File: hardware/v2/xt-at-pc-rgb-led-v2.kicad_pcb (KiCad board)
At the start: 2 copper layers, 54.5 x 33 mm, 25 parts, among them J1 +5V GND, J2 HDD, J3 TURBO, J4 SW IN, J5 SW OUT, J6 ADDR LED (5V DATA GND), J7 RGB LED (COM R G B), J8 ISP, U1 ATtiny84A-PU

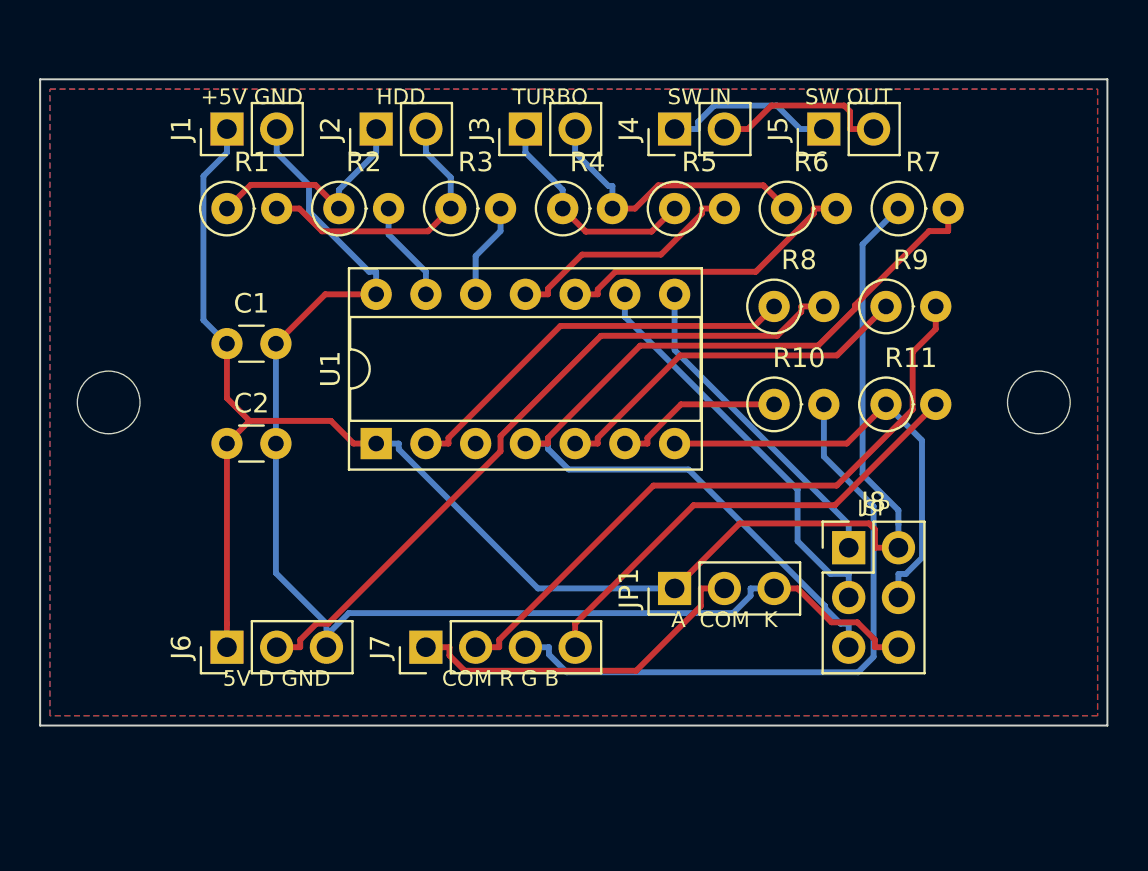
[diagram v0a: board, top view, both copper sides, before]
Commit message: v2: mounting holes between parts, board 42.5 x 33 mm
C2 and R11 moved so the M3 holes fit between the parts; board width
54.5 -> 42.5 mm. Dimension drawings assume standing resistors (about
11 mm height).

Co-Authored-By: Claude Opus 5.5 (1M context) <noreply@anthropic.com>
Claude-Session: https://claude.ai/code/session_01JRatMm8Q7Nvo5CN8dD4gBk
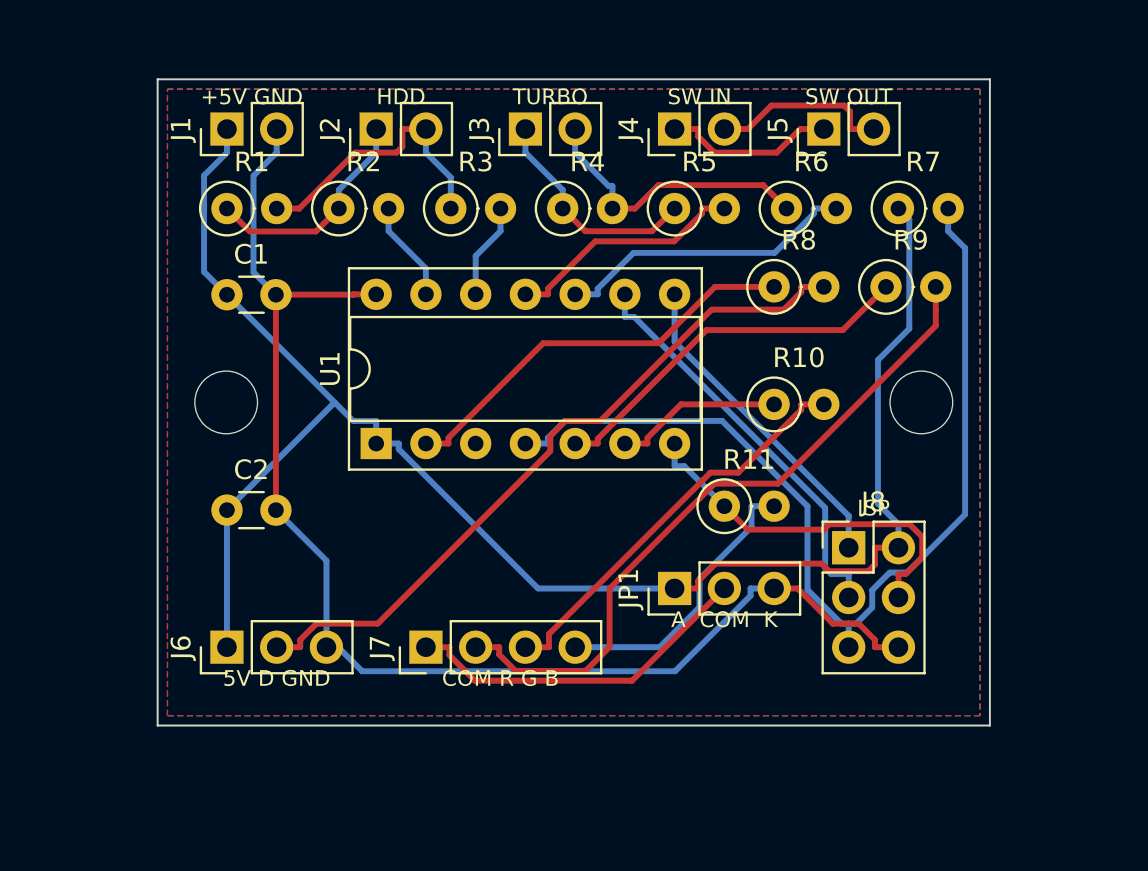
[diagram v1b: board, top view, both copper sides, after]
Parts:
- moved R11 9.76 mm to (127.9, 121.8)
- moved H1 6.00 mm to (102.5, 116.5)
- moved H2 6.00 mm to (138.0, 116.5)
- moved C2 3.40 mm to (102.5, 122.0)
- moved C1 2.50 mm to (102.5, 111.0)
- moved R8 1.00 mm to (130.5, 110.6)
- moved R9 1.00 mm to (136.2, 110.6)
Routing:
- net /LED_G: track 32.8 -> 20.9 mm
- net /LED_B: track 24.3 -> 14.6 mm
- net /PWM_B: track 23.0 -> 19.3 mm
- net /LED_R: track 33.3 -> 35.3 mm
- net GND: track 65.4 -> 67.0 mm
- net /RST: track 49.3 -> 49.9 mm
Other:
- board size 54.5 x 33 mm -> 42.5 x 33 mm

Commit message: Lay resistors and diodes flat on both boards
7.62 mm horizontal footprints, side by side; mounting holes in gaps
between the parts. v1 44 x 25.5 mm, v2 42 x 36.4 mm. Component height
about 8.5 mm.

Co-Authored-By: Claude Opus 5.5 (1M context) <noreply@anthropic.com>
Claude-Session: https://claude.ai/code/session_01JRatMm8Q7Nvo5CN8dD4gBk
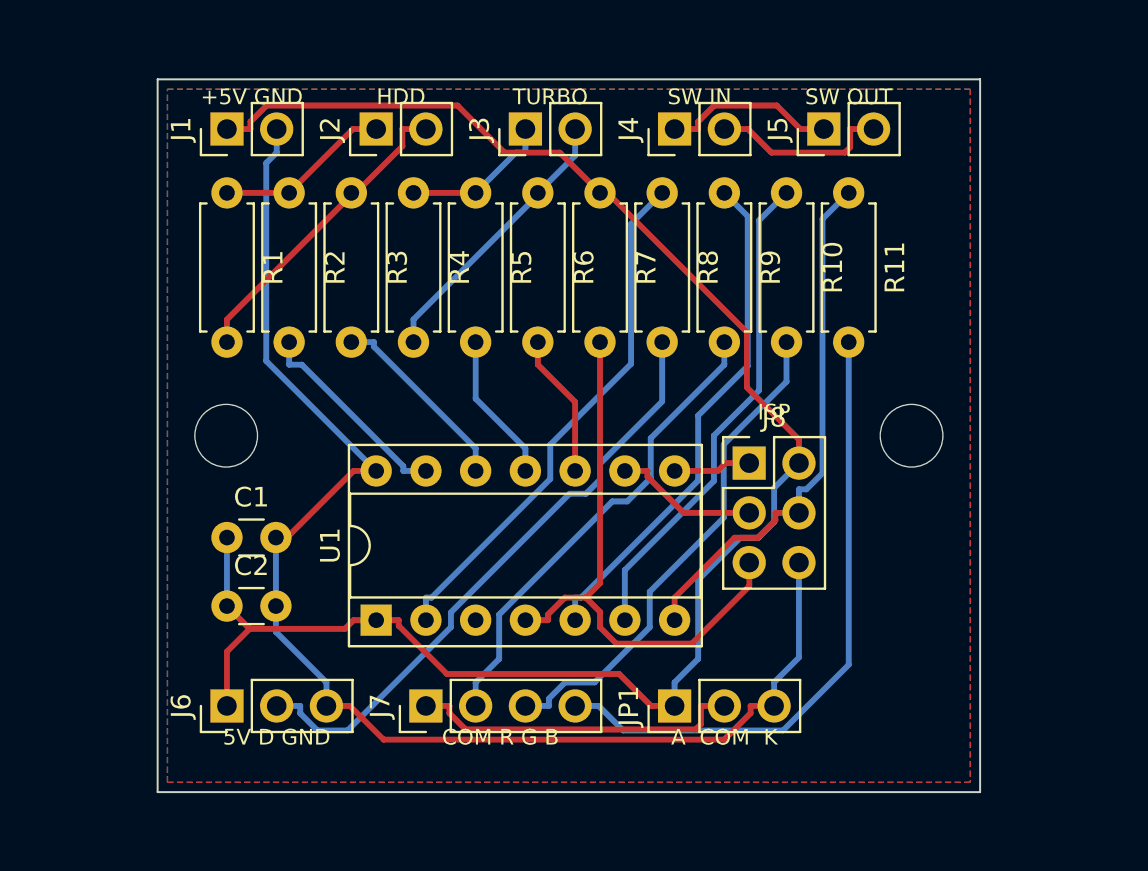
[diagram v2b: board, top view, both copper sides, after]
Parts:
- R1, R10, R11, R2, R3, R4, R5, R6, R7, R8, R9: footprint Resistor_THT:R_Axial_DIN0207_L6.3mm_D2.5mm_P2.54mm_Vertical -> Resistor_THT:R_Axial_DIN0207_L6.3mm_D2.5mm_P7.62mm_Horizontal
- moved R11 17.2 mm to (134.3, 105.8), turned to -90 degrees
- moved R7 15.3 mm to (121.6, 105.8), turned to -90 degrees
- moved R6 12.7 mm to (118.4, 105.8), turned to -90 degrees
- moved C1 12.4 mm to (102.5, 123.4)
- moved R10 10.8 mm to (131.1, 105.8), turned to -90 degrees
- moved R5 10.2 mm to (115.2, 105.8), turned to -90 degrees
- moved R9 9.55 mm to (127.9, 105.8), turned to -90 degrees
- moved U1 9.02 mm to (110.2, 127.6)
- moved R4 7.66 mm to (112.1, 105.8), turned to -90 degrees
- moved R8 7.46 mm to (124.8, 105.8), turned to -90 degrees
- moved J8 6.67 mm to (129.2, 119.6)
- moved JP1 6.00 mm to (125.4, 132.0)
- moved R3 5.14 mm to (108.9, 105.8), turned to -90 degrees
- moved C2 4.90 mm to (102.5, 126.9)
- moved J6 3.00 mm to (102.5, 132.0)
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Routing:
- net /RST: track 49.9 -> 29.3 mm
- net /LED_B: track 14.6 -> 32.4 mm
- net /PWM_G: track 8.62 -> 25.2 mm
- net /SCK: track 21.0 -> 7.41 mm
- net /MISO: track 16.6 -> 3.98 mm
- net /LED_R: track 35.3 -> 24.3 mm
- net /TB_B: track 15.5 -> 7.37 mm
- net /PWM_B: track 19.3 -> 27.1 mm
- net /PWM_R: track 19.3 -> 26.1 mm
- net /DATA_MCU: track 21.3 -> 27.0 mm
- net /HDD_A: track 5.17 -> 10.5 mm
- net /DATA: track 36.4 -> 31.3 mm
- net /HDD_B: track 4.91 -> 9.89 mm
- net /LED_G: track 20.9 -> 25.7 mm
- net /TB_A: track 12.3 -> 7.63 mm
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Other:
- board size 42.5 x 33 mm -> 42 x 36.4 mm

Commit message: More margin above the top labels
1 mm more board above the connector labels so the silkscreen fits;
v1 44 x 26.5 mm, v2 42 x 38.4 mm (holes stay centred).

Co-Authored-By: Claude Opus 5.5 (1M context) <noreply@anthropic.com>
Claude-Session: https://claude.ai/code/session_01JRatMm8Q7Nvo5CN8dD4gBk
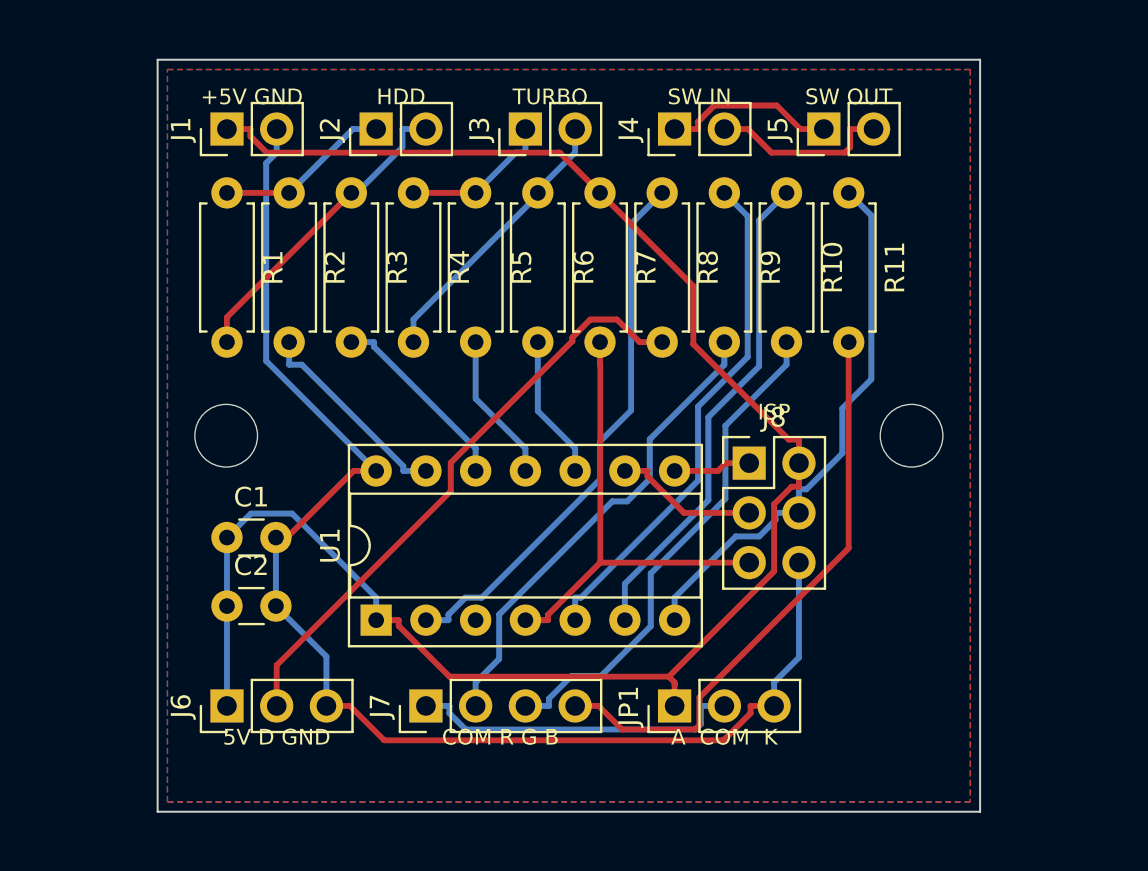
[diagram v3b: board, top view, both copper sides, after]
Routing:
- net /RST: track 29.3 -> 24.1 mm
- net /LED_B: track 32.4 -> 29.7 mm
- net +5V: track 88.8 -> 90.4 mm
- net /DATA_MCU: track 27.0 -> 28.0 mm
- net /PWM_B: track 27.1 -> 28.1 mm
- net /DATA: track 31.3 -> 30.5 mm
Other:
- board size 42 x 36.4 mm -> 42 x 38.4 mm

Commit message: Resistor and diode references inside the body outline
Co-Authored-By: Claude Opus 5.5 (1M context) <noreply@anthropic.com>
Claude-Session: https://claude.ai/code/session_01JRatMm8Q7Nvo5CN8dD4gBk
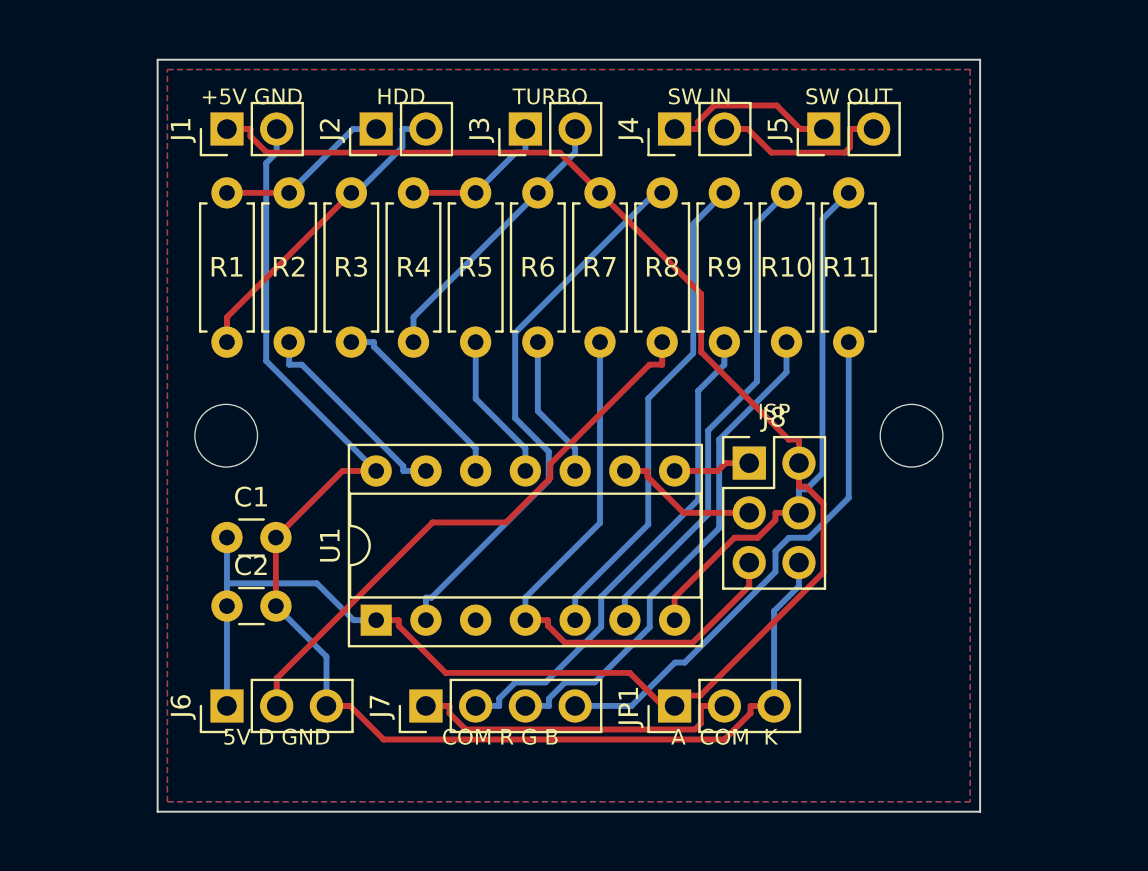
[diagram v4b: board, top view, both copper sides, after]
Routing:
- net /RST: track 24.1 -> 30.3 mm
- net /LED_B: track 29.7 -> 26.9 mm
- net /DATA: track 30.5 -> 29.3 mm
- net /PWM_R: track 26.1 -> 25.0 mm
- net /LED_R: track 24.3 -> 25.4 mm
- net /PWM_B: track 28.1 -> 27.1 mm
- net /DATA_MCU: track 28.0 -> 28.6 mm

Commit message: v2: more margin, lower bottom labels; references along the parts
v2 42 x 40.4 mm: 1 mm more above the top labels, bottom connector
labels 2 mm lower. Resistor and diode references run along the body
on both boards.

Co-Authored-By: Claude Opus 5.5 (1M context) <noreply@anthropic.com>
Claude-Session: https://claude.ai/code/session_01JRatMm8Q7Nvo5CN8dD4gBk
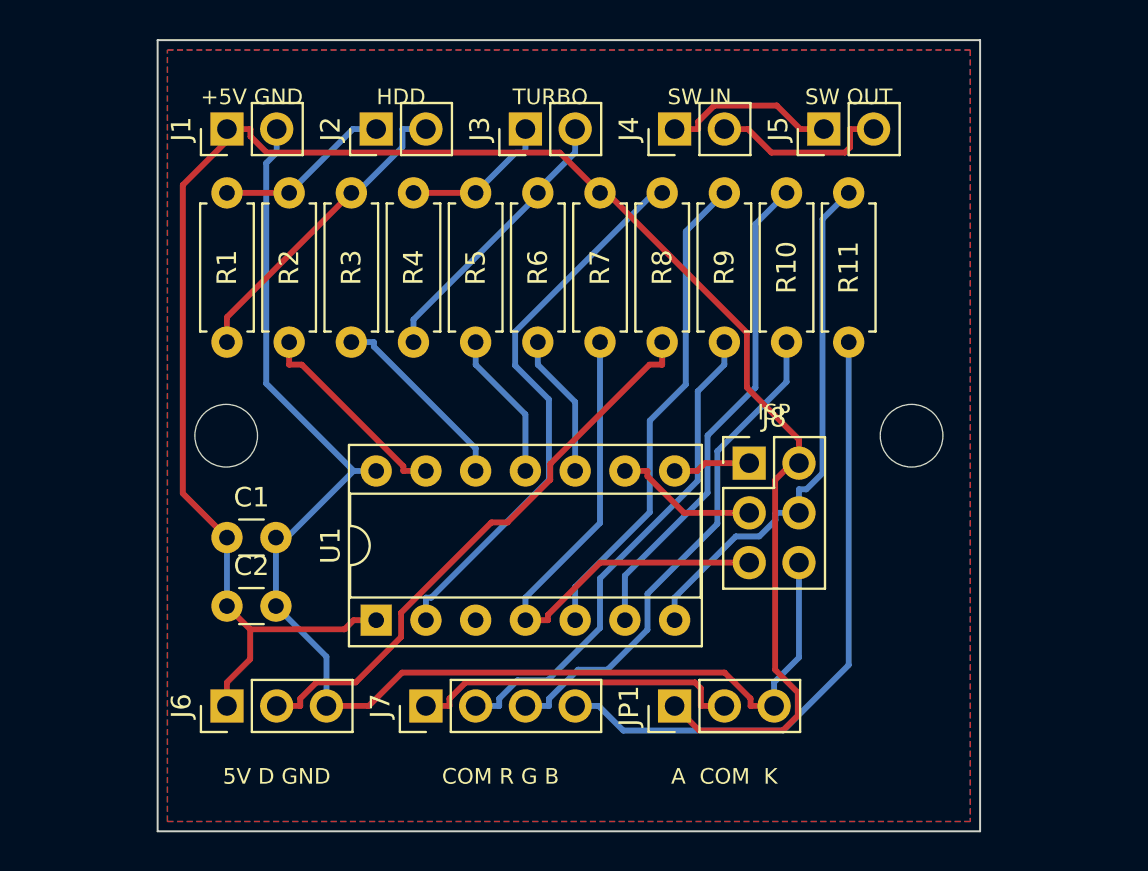
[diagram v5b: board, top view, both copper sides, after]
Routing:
- net +5V: track 90.5 -> 99.4 mm
- net /LED_B: track 26.9 -> 32.4 mm
- net /RST: track 30.3 -> 28.6 mm
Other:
- board size 42 x 38.4 mm -> 42 x 40.4 mm
